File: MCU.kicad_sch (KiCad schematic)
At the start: 12 parts, among them U201 ESP32-S3-PICO-1-N8R2

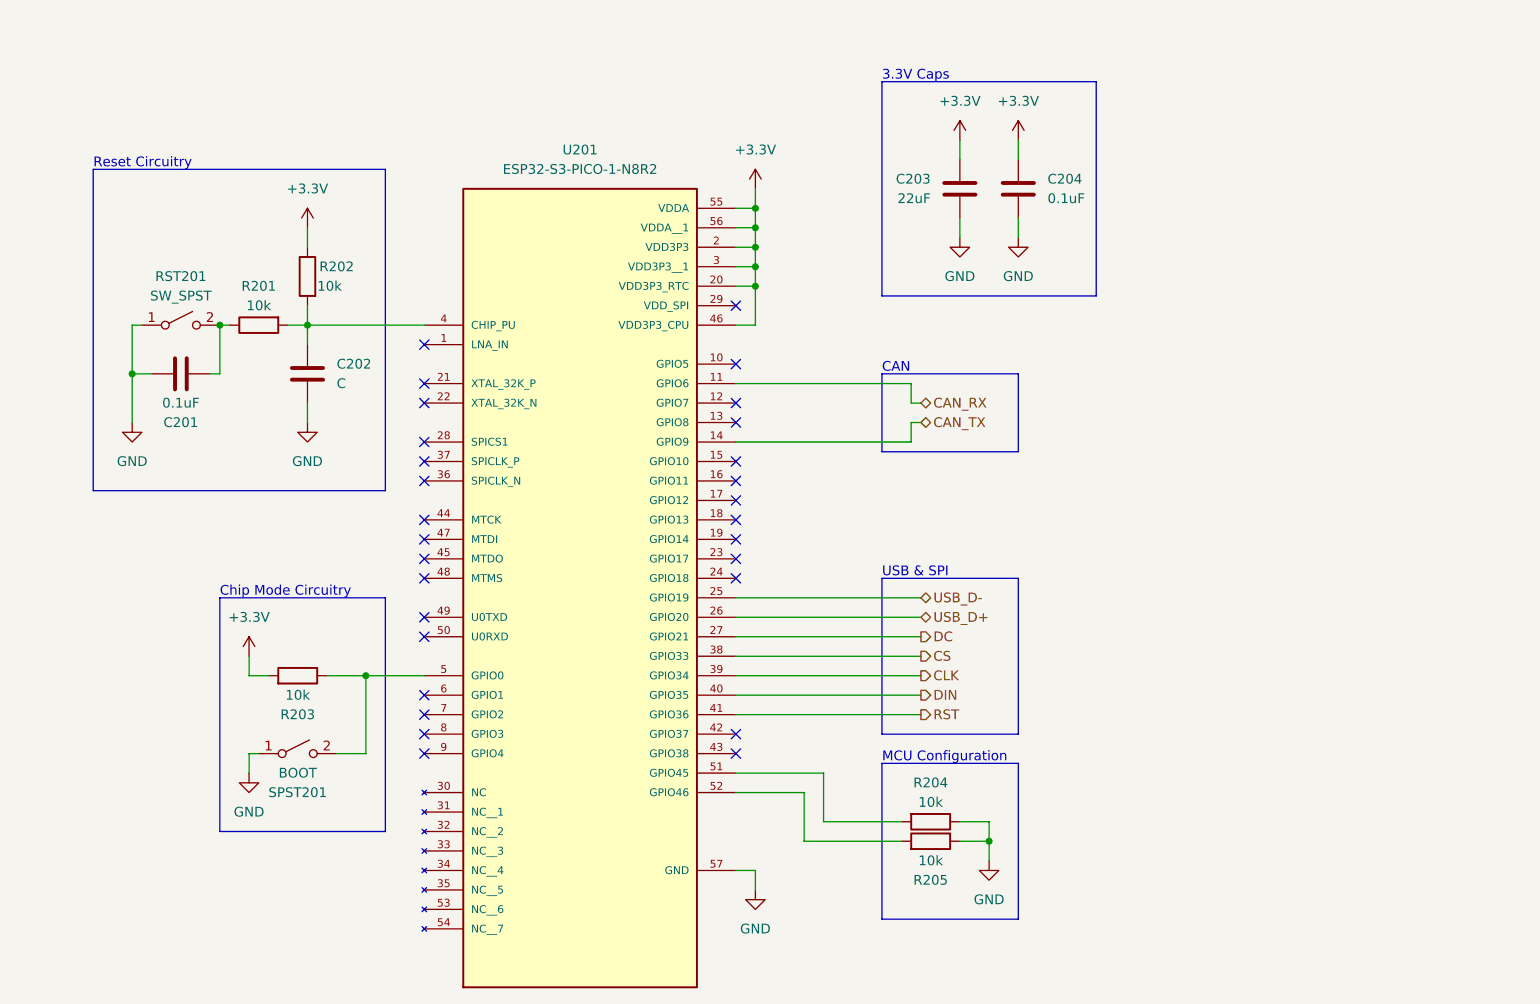
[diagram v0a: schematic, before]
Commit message: Reworked DisplayBoard circuitry and layout; v1.1
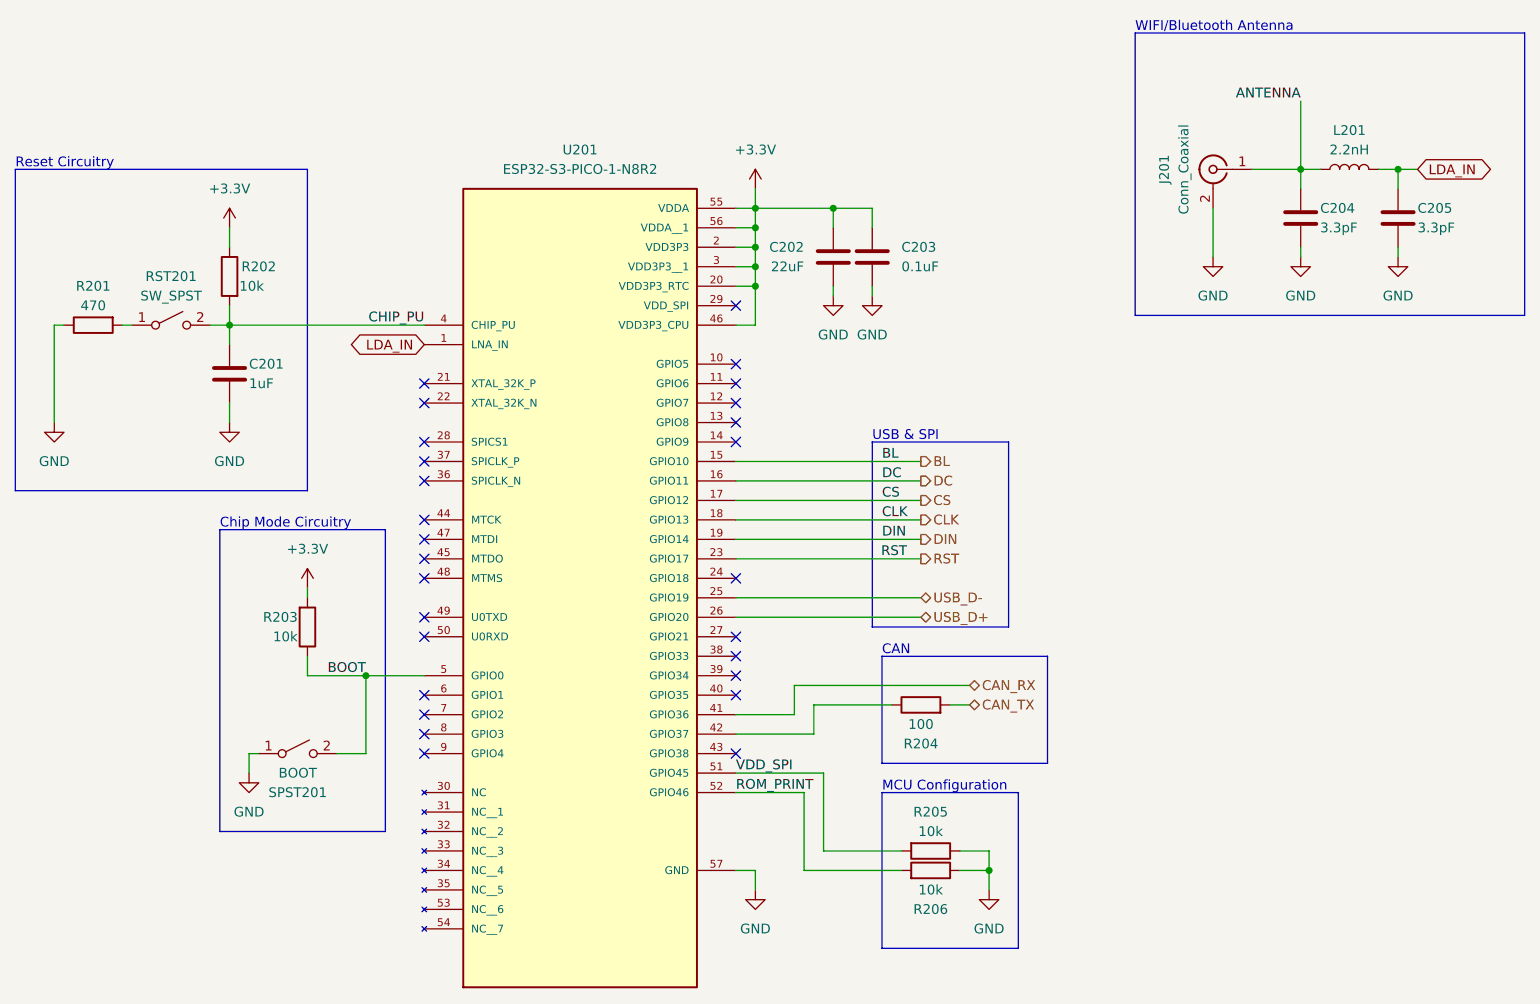
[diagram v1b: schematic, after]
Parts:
- removed C201: 0.1uF, Capacitor_SMD:C_0805_2012Metric, symbol Device:C
- added C204, C205: 3.3pF, Capacitor_SMD:C_0603_1608Metric, symbol Device:C
- added J201: Conn_Coaxial, CustomFootprints:CONMHF1-SMD-G-T_U.FL, symbol Connector:Conn_Coaxial
- added L201: 2.2nH, Inductor_SMD:L_0603_1608Metric, symbol Device:L
- added R204: 100, Resistor_SMD:R_0603_1608Metric, symbol Device:R
- C201: renamed from C202; value C -> 1uF
- R201: value 10k -> 470
- RST201, SPST201: footprint TS-1088-AR02016:SMD_Push_Button -> CustomFootprints:XUNPU_Button
- U201: footprint ESP32-S3-PICO-1:PQFN40P700X700X106-57N -> CustomFootprints:ESP32-S3-PICO-1
- renumbered C203 to C202, C204 to C203, R204 to R205, R205 to R206
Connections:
- net CAN_RX: now also U201.41 (GPIO36); no longer U201.11 (GPIO6)
- net CAN_TX: now also R204.2; no longer U201.14 (GPIO9)
- net CLK: now also U201.18 (GPIO13); no longer U201.39 (GPIO34)
- net CS: now also U201.17 (GPIO12); no longer U201.38 (GPIO33)
- net DC: now also U201.16 (GPIO11); no longer U201.27 (GPIO21)
- net DIN: now also U201.19 (GPIO14); no longer U201.40 (GPIO35)
- net GND: now also R201.1, C204.2, C205.2, J201.2 (Ext); no longer RST201.1 (A)
- net RST: now also U201.23 (GPIO17); no longer U201.41 (GPIO36)
- net ROM_PRINT: now reaches R206.2, U201.52 (GPIO46)
- net CHIP_PU: now reaches RST201.2 (B)
- net CHIP_PU: now also C201.1, R202.2, U201.4 (CHIP_PU); no longer R201.1
- net LDA_IN: now reaches U201.1 (LNA_IN)
- net LDA_IN: now also C205.1, L201.2
- net BL: now reaches U201.15 (GPIO10)
- net at U201.42 (GPIO37): now also R204.1
- net BOOT: now reaches R203.1, SPST201.2 (B), U201.5 (GPIO0)
- net VDD_SPI: now reaches R205.2, U201.51 (GPIO45)
- new net: R201.2, RST201.1 (A)
- new net ANTENNA: C204.1, J201.1 (In), L201.1
- no-connect marks 29 -> 27
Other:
- note added: "WIFI/Bluetooth Antenna"
- note removed: "3.3V Caps"
- moved on the sheet: C201, C202, C203, R201, R202, R203, R205, R206, RST201

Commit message: Finished v1.1
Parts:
- removed U201: ESP32-S3-PICO-1-N8R2, CustomFootprints:ESP32-S3-PICO-1, symbol ESP32-S3-PICO-1-N8R2:ESP32-S3-PICO-1-N8R2
- added U1: ESP32-S3-PICO-1-N8R2, CustomFootprints:ESP32-S3-PICO-1, symbol CustomSymbols:ESP32-S3-PICO-1-N8R2
- C3: renamed from C203; value 0.1uF -> 100nF
- renumbered C201 to C1, C202 to C2, C204 to C4, C205 to C5, J201 to J1, L201 to L1, R201 to R1, R203 to R2, R202 to R3, R204 to R4, R205 to R5, R206 to R6, RST201 to RST1, SPST201 to SPST1
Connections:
- net +3.3V: now also U1.2 (VDD3P3), U1.20 (VDD3P3_RTC), U1.3 (VDD3P3__1), U1.46 (VDD3P3_CPU), U1.55 (VDDA), U1.56 (VDDA__1)
- net BL: now also U1.12 (GPIO7)
- net BOOT: now also U1.5 (GPIO0)
- net CAN_RX: now also U1.44 (MTCK)
- net CHIP_PU: now also U1.4 (CHIP_PU)
- net CLK: now also U1.15 (GPIO10)
- net CS: now also U1.13 (GPIO8)
- net GND: now also U1.57 (GND)
- net LDA_IN: now also U1.1 (LNA_IN)
- net ROM_PRINT: now also U1.52 (GPIO46)
- net RST: now also U1.14 (GPIO9)
- net USB_D+: now also U1.26 (GPIO20)
- net USB_D-: now also U1.25 (GPIO19)
- net VDD_SPI: now also U1.51 (GPIO45)
- net at R4.1: now also U1.45 (MTDO)
- new net IO0: U1.19 (GPIO14)
- new net IO1: U1.18 (GPIO13)
- new net IO2: U1.17 (GPIO12)
- new net IO3: U1.16 (GPIO11)
- new net TE: U1.24 (GPIO18)
- no-connect marks 27 -> 24
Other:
- note added: "SPI"
- note added: "USB"
- note removed: "USB & SPI"
- moved on the sheet: C2, C3, R2, R4, SPST1
